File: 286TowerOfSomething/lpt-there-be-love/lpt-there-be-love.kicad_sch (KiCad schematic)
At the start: 1 part, among them J1 Bus_ISA_16bit

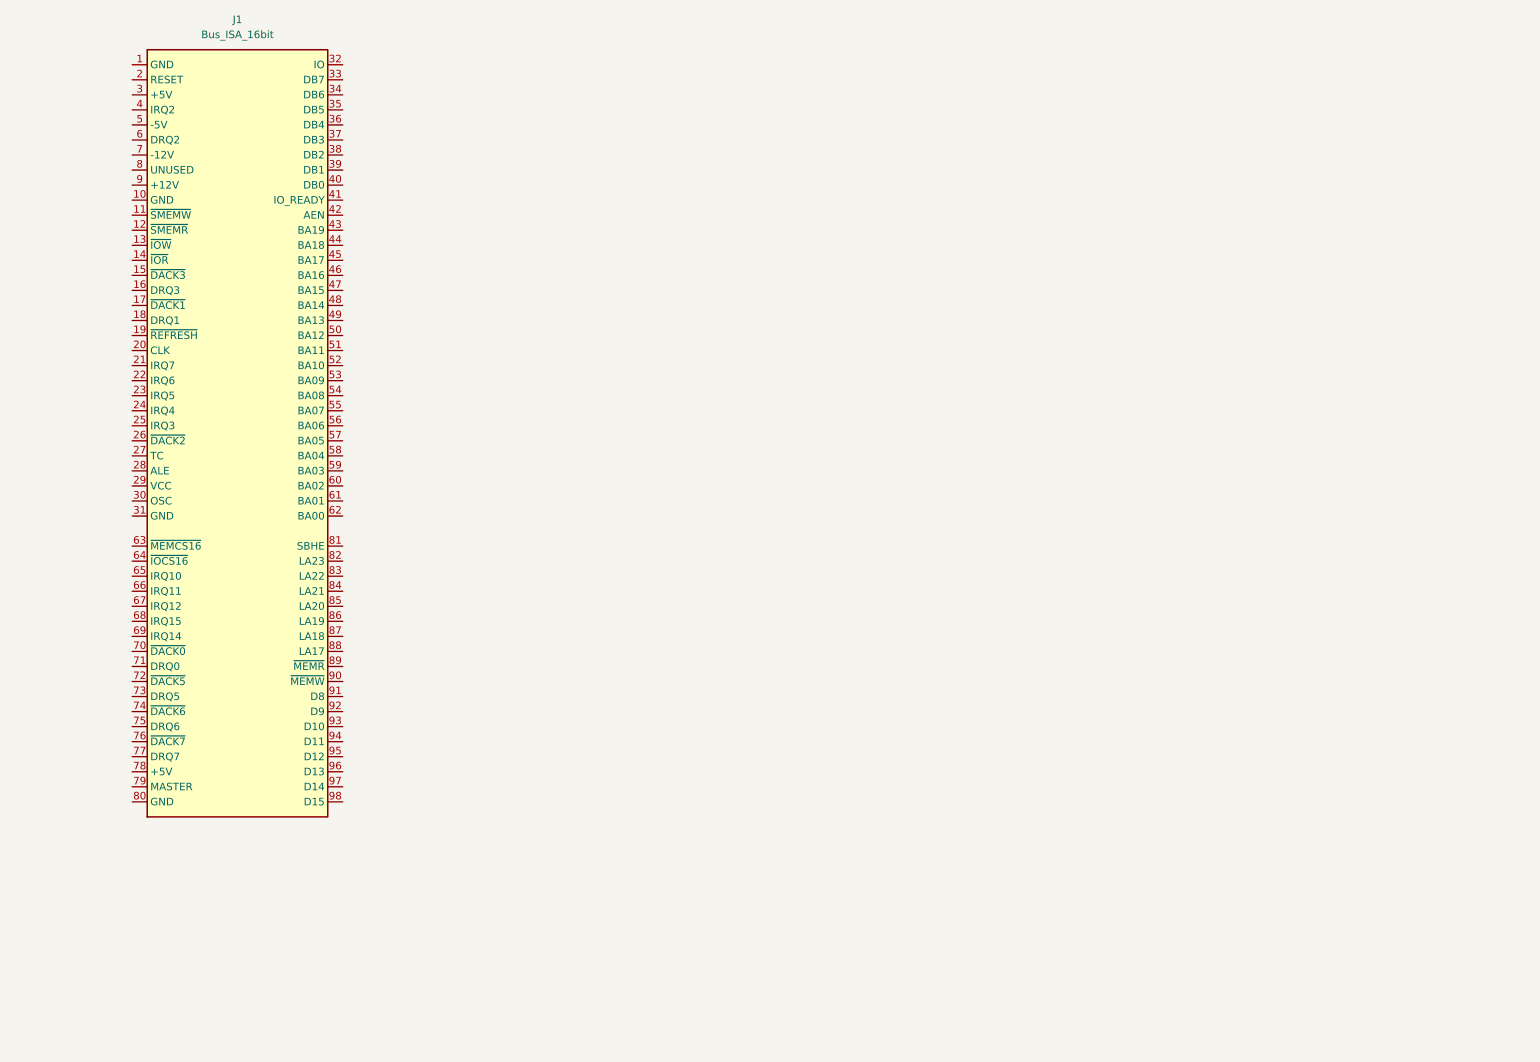
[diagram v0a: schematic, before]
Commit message: lpt-there-be-love schematic is at about 85% - added parport ASIC symbol and most of the schematic was doneat that point
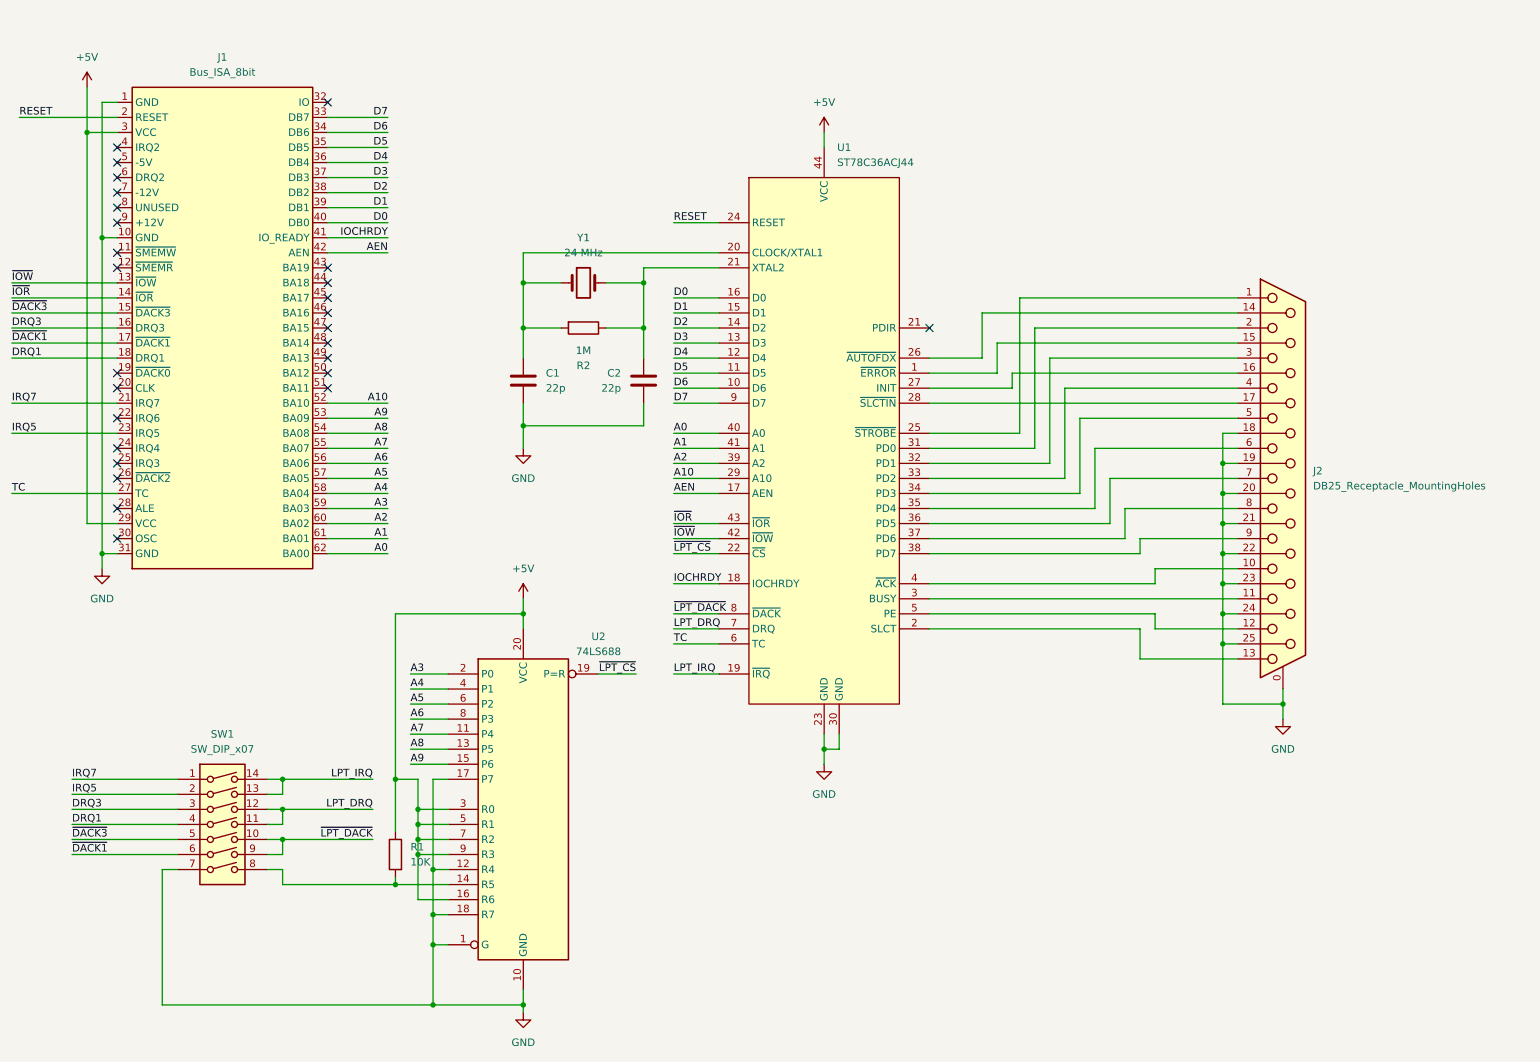
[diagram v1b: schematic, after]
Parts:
- removed J1: Bus_ISA_16bit, symbol Connector:Bus_ISA_16bit
- added C1, C2: 22p, symbol Device:C
- added J1: Bus_ISA_8bit, pc-parts:BUS_AT_8BIT, symbol Connector:Bus_ISA_8bit
- added J2: DB25_Receptacle_MountingHoles, symbol Connector:DB25_Receptacle_MountingHoles
- added R1: 10K, symbol Device:R
- added R2: 1M, symbol Device:R
- added SW1: SW_DIP_x07, Button_Switch_THT:SW_DIP_SPSTx07_Slide_9.78x19.96mm_W7.62mm_P2.54mm, symbol Switch:SW_DIP_x07
- added U1: ST78C36ACJ44, Package_LCC:PLCC-44_THT-Socket, symbol pc-parts:ST78C36ACJ44
- added U2: 74LS688, Package_DIP:DIP-20_W7.62mm, symbol 74xx:74LS688
- added Y1: 24 MHz, symbol Device:Crystal
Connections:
- new net: C1.1, R2.2, U1.20 (CLOCK/XTAL1), Y1.1
- new net: C2.1, R2.1, U1.21 (XTAL2), Y1.2
- new net: J2.15 (P15), U1.1 (~{ERROR})
- new net: J2.13, U1.2 (SLCT)
- new net: J2.1, U1.25 (~{STROBE})
- new net: J2.14 (P14), U1.26 (~{AUTOFDX})
- new net: J2.16 (P16), U1.27 (INIT)
- new net: J2.17 (P17), U1.28 (~{SLCTIN})
- new net: J2.11, U1.3 (BUSY)
- new net: J2.2, U1.31 (PD0)
- new net: J2.3, U1.32 (PD1)
- new net: J2.4, U1.33 (PD2)
- new net: J2.5, U1.34 (PD3)
- new net: J2.6, U1.35 (PD4)
- new net: J2.7, U1.36 (PD5)
- new net: J2.8, U1.37 (PD6)
- new net: J2.9, U1.38 (PD7)
- new net: J2.10, U1.4 (~{ACK})
- new net: J2.12, U1.5 (PE)
- new net: R1.2, SW1.8, U2.14 (R5)
- new net +5V: J1.29 (VCC), J1.3 (VCC), R1.1, U1.44 (VCC), U2.16 (R6), U2.20 (VCC), U2.3 (R0), U2.5 (R1), U2.7 (R2), U2.9 (R3)
- new net A0: J1.62 (BA00), U1.40 (A0)
- new net A1: J1.61 (BA01), U1.41 (A1)
- new net A10: J1.52 (BA10), U1.29 (A10)
- new net A2: J1.60 (BA02), U1.39 (A2)
- new net A3: J1.59 (BA03), U2.2 (P0)
- new net A4: J1.58 (BA04), U2.4 (P1)
- new net A5: J1.57 (BA05), U2.6 (P2)
- new net A6: J1.56 (BA06), U2.8 (P3)
- new net A7: J1.55 (BA07), U2.11 (P4)
- new net A8: J1.54 (BA08), U2.13 (P5)
- new net A9: J1.53 (BA09), U2.15 (P6)
- new net AEN: J1.42 (AEN), U1.17 (AEN)
- new net D0: J1.40 (DB0), U1.16 (D0)
- new net D1: J1.39 (DB1), U1.15 (D1)
- new net D2: J1.38 (DB2), U1.14 (D2)
- new net D3: J1.37 (DB3), U1.13 (D3)
- new net D4: J1.36 (DB4), U1.12 (D4)
- new net D5: J1.35 (DB5), U1.11 (D5)
- new net D6: J1.34 (DB6), U1.10 (D6)
- new net D7: J1.33 (DB7), U1.9 (D7)
- new net DRQ1: J1.18 (DRQ1), SW1.4
- new net DRQ3: J1.16 (DRQ3), SW1.3
- new net GND: C1.2, C2.2, J1.1 (GND), J1.10 (GND), J1.31 (GND), J2.0 (PAD), J2.18 (P18), J2.19 (P19), J2.20 (P20), J2.21 (P21), J2.22 (P22), J2.23 (P23), J2.24 (P24), J2.25 (P25), SW1.7, U1.23 (GND), U1.30 (GND), U2.1 (G), U2.10 (GND), U2.12 (R4), U2.17 (P7), U2.18 (R7)
- new net IOCHRDY: J1.41 (IO_READY), U1.18 (IOCHRDY)
- new net IRQ5: J1.23 (IRQ5), SW1.2
- new net IRQ7: J1.21 (IRQ7), SW1.1
- new net LPT_DRQ: SW1.11, SW1.12, U1.7 (DRQ)
- new net LPT_IRQ: SW1.13, SW1.14, U1.19 (~{IRQ})
- new net RESET: J1.2 (RESET), U1.24 (RESET)
- new net TC: J1.27 (TC), U1.6 (TC)
- new net ~{DACK1}: J1.17 (~{DACK1}), SW1.6
- new net ~{DACK3}: J1.15 (~{DACK3}), SW1.5
- new net ~{IOR}: J1.14 (~{IOR}), U1.43 (~{IOR})
- new net ~{IOW}: J1.13 (~{IOW}), U1.42 (~{IOW})
- new net ~{LPT_CS}: U1.22 (~{CS}), U2.19 (P=R)
- new net ~{LPT_DACK}: SW1.10, SW1.9, U1.8 (~{DACK})
- no-connect marks 0 -> 27
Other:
- company: (none) -> Surreality Labs
- title: (none) -> LPT There Be Love

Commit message: Started board layout for lpt-there-be-love
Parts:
- added H1, H2: MountingHole, MountingHole:MountingHole_3.2mm_M3_DIN965, symbol Mechanical:MountingHole
- C1, C2: footprint (none) -> Capacitor_SMD:C_0603_1608Metric_Pad1.08x0.95mm_HandSolder
- J2: footprint (none) -> Connector_Dsub:DSUB-25_Female_Horizontal_P2.77x2.84mm_EdgePinOffset4.94mm_Housed_MountingHolesOffset7.48mm
- R1, R2: footprint (none) -> Resistor_SMD:R_0603_1608Metric_Pad0.98x0.95mm_HandSolder
- Y1: footprint (none) -> Crystal:Crystal_HC49-U_Vertical
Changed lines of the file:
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@@
 			)
 		)
-		(property "Footprint" ""
+		(property "Footprint" "Capacitor_SMD:C_0603_1608Metric_Pad1.08x0.95mm_HandSolder"
 			(at 102.5652 88.9 0)
 			(effects
@@
 			)
 		)
-		(property "Footprint" ""
+		(property "Footprint" "Capacitor_SMD:C_0603_1608Metric_Pad1.08x0.95mm_HandSolder"
 			(at 120.9548 88.9 0)
 			(effects
@@
 	)
 	(symbol
+		(lib_id "Mechanical:MountingHole")
+		(at 127 182.88 0)
+		(unit 1)
+		(exclude_from_sim yes)
+		(in_bom no)
+		(on_board yes)
+		(dnp no)
+		(fields_autoplaced yes)
+		(property "Reference" "H2"
+			(at 129.54 181.6099 0)
+			(effects
+				(font
+					(size 1.27 1.27)
+				)
+				(justify left)
+			)
+		)
+		(property "Value" "MountingHole"
+			(at 129.54 184.1499 0)
+			(effects
+				(font
+					(size 1.27 1.27)
+				)
+				(justify left)
+			)
+		)
+		(property "Footprint" "MountingHole:MountingHole_3.2mm_M3_DIN965"
+			(at 127 182.88 0)
+			(effects
+				(font
+					(size 1.27 1.27)
+				)
+				(hide yes)
+			)
+		)
+		(property "Datasheet" "~"
+			(at 127 182.88 0)
+			(effects
+				(font
+					(size 1.27 1.27)
+				)
+				(hide yes)
+			)
+		)
+		(property "Description" "Mounting Hole without connection"
+			(at 127 182.88 0)
+			(effects
+				(font
+					(size 1.27 1.27)
+				)
+				(hide yes)
+			)
+		)
+		(instances
+			(project "lpt-there-be-love"
+				(path "/d5262cac-9e9d-4409-be22-17aefab615fa"
+					(reference "H2")
+					(unit 1)
+				)
+			)
+		)
+	)
+	(symbol
 		(lib_id "power:GND")
 		(at 101.6 96.52 0)
@@
 			)
 		)
-		(property "Footprint" ""
+		(property "Footprint" "Crystal:Crystal_HC49-U_Vertical"
 			(at 111.76 68.58 0)
 			(effects
@@
 			)
 		)
-		(property "Footprint" ""
+		(property "Footprint" "Connector_Dsub:DSUB-25_Female_Horizontal_P2.77x2.84mm_EdgePinOffset4.94mm_Housed_MountingHolesOffset7.48mm"
 			(at 229.87 101.6 0)
 			(effects
@@
 			)
 		)
-		(property "Footprint" ""
+		(property "Footprint" "Resistor_SMD:R_0603_1608Metric_Pad0.98x0.95mm_HandSolder"
 			(at 81.788 165.1 90)
 			(effects
@@
 	)
 	(symbol
+		(lib_id "Mechanical:MountingHole")
+		(at 127 177.8 0)
+		(unit 1)
+		(exclude_from_sim yes)
+		(in_bom no)
+		(on_board yes)
+		(dnp no)
+		(fields_autoplaced yes)
+		(property "Reference" "H1"
+			(at 129.54 176.5299 0)
+			(effects
+				(font
+					(size 1.27 1.27)
+				)
+				(justify left)
+			)
+		)
+		(property "Value" "MountingHole"
+			(at 129.54 179.0699 0)
+			(effects
+				(font
+					(size 1.27 1.27)
+				)
+				(justify left)
+			)
+		)
+		(property "Footprint" "MountingHole:MountingHole_3.2mm_M3_DIN965"
+			(at 127 177.8 0)
+			(effects
+				(font
+					(size 1.27 1.27)
+				)
+				(hide yes)
+			)
+		)
+		(property "Datasheet" "~"
+			(at 127 177.8 0)
+			(effects
+				(font
+					(size 1.27 1.27)
+				)
+				(hide yes)
+			)
+		)
+		(property "Description" "Mounting Hole without connection"
+			(at 127 177.8 0)
+			(effects
+				(font
+					(size 1.27 1.27)
+				)
+				(hide yes)
+			)
+		)
+		(instances
+			(project ""
+				(path "/d5262cac-9e9d-4409-be22-17aefab615fa"
+					(reference "H1")
+					(unit 1)
+				)
+			)
+		)
+	)
+	(symbol
 		(lib_id "Device:R")
 		(at 111.76 76.2 270)
@@
 			)
 		)
-		(property "Footprint" ""
+		(property "Footprint" "Resistor_SMD:R_0603_1608Metric_Pad0.98x0.95mm_HandSolder"
 			(at 111.76 74.422 90)
 			(effects

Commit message: Layout of lpt-there-be-love just about done
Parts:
- removed H1, H2: MountingHole, MountingHole:MountingHole_3.2mm_M3_DIN965, symbol Mechanical:MountingHole
- added C10, C11, C12, C13, C14, C15, C16, C17, C18, C19, C20, C21, C22, C23, C7, C8, C9: 180p, Capacitor_SMD:C_0603_1608Metric_Pad1.08x0.95mm_HandSolder, symbol Device:C
- added C3, C4: 100n, Capacitor_SMD:C_0603_1608Metric_Pad1.08x0.95mm_HandSolder, symbol Device:C
- added C5: 1u, Capacitor_SMD:C_0805_2012Metric_Pad1.18x1.45mm_HandSolder, symbol Device:C
- added C6: 22u, Capacitor_SMD:CP_Elec_5x5.3, symbol Device:C_Polarized
- added R3, R4, R5, R6, R7: 4.7K, Resistor_SMD:R_0603_1608Metric_Pad0.98x0.95mm_HandSolder, symbol Device:R
- J2: value DB25_Receptacle_MountingHoles -> DB25F
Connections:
- net +5V: now also C3.1, C4.1, C5.1, C6.1, R3.1, R4.1, R5.1, R6.1, R7.1
- net GND: now also C10.2, C11.2, C12.2, C13.2, C14.2, C15.2, C16.2, C17.2, C18.2, C19.2, C20.2, C21.2, C22.2, C23.2, C3.2, C4.2, C5.2, C6.2, C7.2, C8.2, C9.2
- net at J2.15 (P15), U1.1 (~{ERROR}): now also C22.1, R4.2
- net at J2.13, U1.2 (SLCT): now also C23.1
- net at J2.1, U1.25 (~{STROBE}): now also C19.1, R7.2
- net at J2.14 (P14), U1.26 (~{AUTOFDX}): now also C7.1, R3.2
- net at J2.16 (P16), U1.27 (INIT): now also C21.1, R5.2
- net at J2.17 (P17), U1.28 (~{SLCTIN}): now also C20.1, R6.2
- net at J2.11, U1.3 (BUSY): now also C9.1
- net at J2.2, U1.31 (PD0): now also C18.1
- net at J2.3, U1.32 (PD1): now also C17.1
- net at J2.4, U1.33 (PD2): now also C16.1
- net at J2.5, U1.34 (PD3): now also C15.1
- net at J2.6, U1.35 (PD4): now also C14.1
- net at J2.7, U1.36 (PD5): now also C13.1
- net at J2.8, U1.37 (PD6): now also C12.1
- net at J2.9, U1.38 (PD7): now also C11.1
- net at J2.10, U1.4 (~{ACK}): now also C10.1
- net at J2.12, U1.5 (PE): now also C8.1
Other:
- moved on the sheet: J2

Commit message: Adding proper bracket to lpt-there-be-love
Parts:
- added BRACKET1: ~, pc-parts:PC_BRACKET_ISA_KEYSTONE_9200_Rev1_1, symbol pc-parts:9202
- J2: footprint Connector_Dsub:DSUB-25_Female_Horizontal_P2.77x2.84mm_EdgePinOffset4.94mm_Housed_MountingHolesOffset7.48mm -> Connector_Dsub:DSUB-25_Female_Horizontal_P2.77x2.84mm_EdgePinOffset4.94mm_Housed_MountingHolesOffset4.94mm
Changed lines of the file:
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@@
 			)
 		)
-		(property "Footprint" "Connector_Dsub:DSUB-25_Female_Horizontal_P2.77x2.84mm_EdgePinOffset4.94mm_Housed_MountingHolesOffset7.48mm"
+		(property "Footprint" "Connector_Dsub:DSUB-25_Female_Horizontal_P2.77x2.84mm_EdgePinOffset4.94mm_Housed_MountingHolesOffset4.94mm"
 			(at 255.27 101.6 0)
 			(effects
@@
 					(unit 1)
 				)
+			)
+		)
+	)
+	(symbol
+		(lib_id "pc-parts:9202")
+		(at 139.7 190.5 0)
+		(unit 1)
+		(exclude_from_sim no)
+		(in_bom yes)
+		(on_board yes)
+		(dnp no)
+		(fields_autoplaced yes)
+		(property "Reference" "BRACKET1"
+			(at 139.7 190.5 0)
+			(effects
+				(font
+					(size 1.27 1.27)
+				)
+				(hide yes)
+			)
+		)
+		(property "Value" "~"
+			(at 144.78 190.5 0)
+			(effects
+				(font
+					(size 1.27 1.27)
+				)
+				(justify left)
+			)
+		)
+		(property "Footprint" "pc-parts:PC_BRACKET_ISA_KEYSTONE_9200_Rev1_1"
+			(at 139.7 190.5 0)
+			(effects
+				(font
+					(size 1.27 1.27)
+				)
+				(hide yes)
+			)
+		)
+		(property "Datasheet" ""
+			(at 139.7 190.5 0)
+			(effects
+				(font
+					(size 1.27 1.27)
+				)
+				(hide yes)
+			)
+		)
+		(property "Description" ""
+			(at 139.7 190.5 0)
+			(effects
+				(font
+					(size 1.27 1.27)
+				)
+				(hide yes)
+			)
+		)
+		(instances
+			(project ""
+				(path "/d5262cac-9e9d-4409-be22-17aefab615fa"
+					(reference "BRACKET1")
+					(unit 1)
+				)
